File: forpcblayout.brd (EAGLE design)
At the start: 105.5 x 66.3 mm, 89 parts, among them J1 3x2 M, J2 S2B-PH-SM4-TB(LF)(SN), J3 629105136821, SW1 AYZ0202AGRLC, SW2 !RESET, T1 2N2222, T2 2N2222, T3 2N2222, T4 2N2222, U1 MCP73831, U2 MIC5219, U3 ATMEGA32U4-AUR, X2 16 MHz

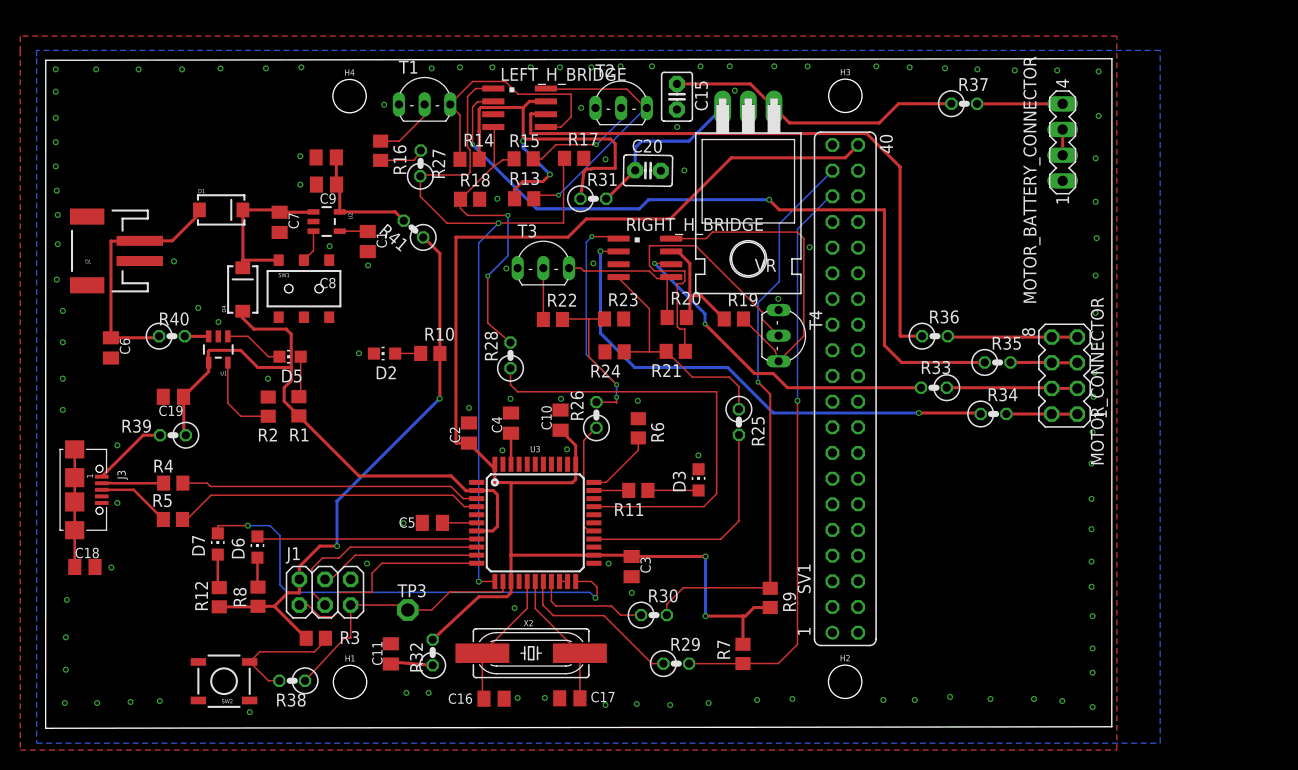
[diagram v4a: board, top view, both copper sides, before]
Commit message: Changed just about everything
Jk, changed wire widths, stitched properly, passed ERC as well as DRC
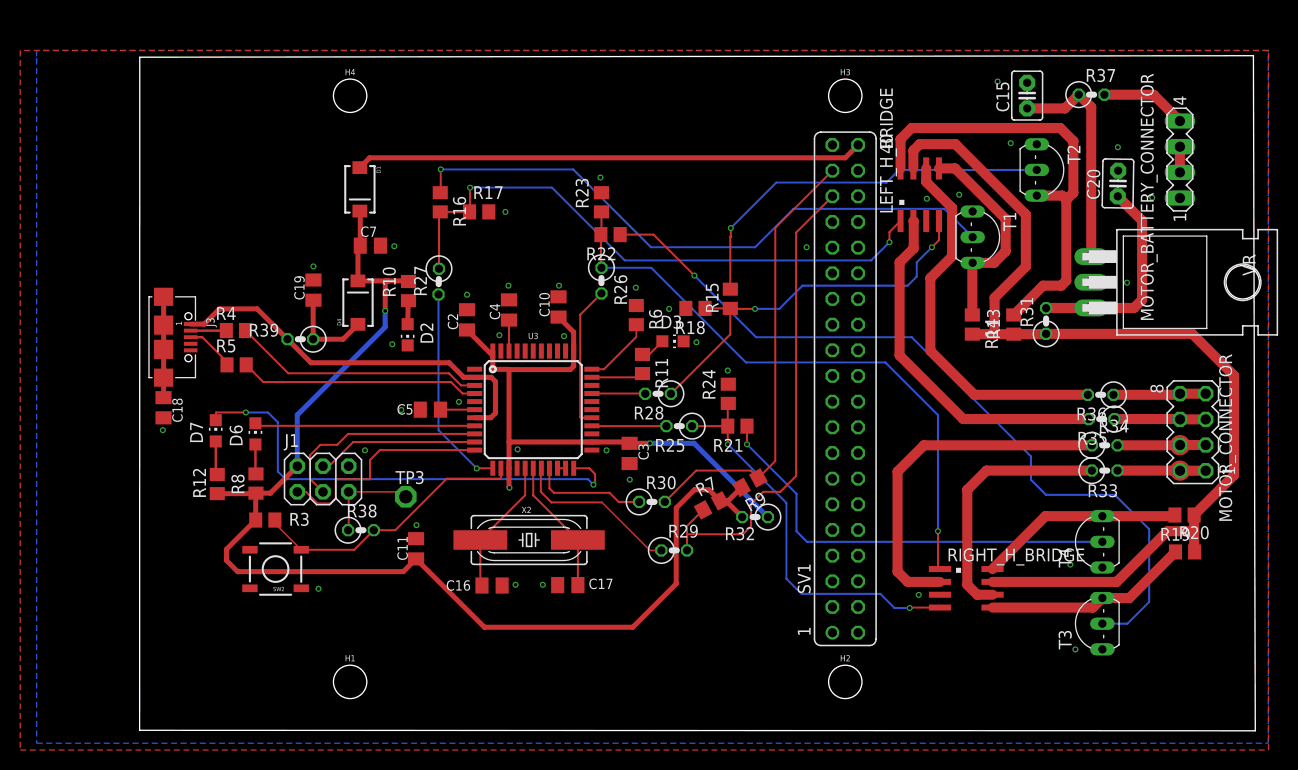
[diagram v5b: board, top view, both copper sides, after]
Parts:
- removed C1: 470p, rcl:C0805K
- removed C6, C8: 4.7u, rcl:C0805K
- removed C9: 100n, rcl:C0805K
- removed D5: GREEN, led:CHIP-LED0805
- removed J2: S2B-PH-SM4-TB(LF)(SN), SparkFun-Connectors:JST-2-SMD
- removed R1: 1K, rcl:R0805
- removed R2: 10K, rcl:R0805
- removed R40, R41: 0, rcl:0207/2V
- removed SW1: AYZ0202AGRLC, SparkFun-Electromechanical:AYZ0202
- removed U1: MCP73831, SparkFun-PowerIC:SOT23-5
- removed U2: MIC5219, SparkFun-PowerIC:SOT23-5
- MOTOR_BATTERY_CONNECTOR: value (none) -> MOTOR_BATTERY_CONNECTOR
- MOTOR_CONNECTOR: value (none) -> MOTOR_CONNECTOR
- R7, R9: value 1K -> 4.7K
- SV1: value (none) -> EXTENDED PIN HEADER
- moved T3 65.2 mm to (103.3, 10.3), turned to 90 degrees
- moved T1 57.3 mm to (93.0, 48.6), turned to 270 degrees
- moved R20 55.4 mm to (112.8, 17.4)
- moved R14 52.4 mm to (91.7, 40.0), turned to 270 degrees
- moved R13 50.0 mm to (95.8, 40.0), turned to 90 degrees
- moved R19 48.6 mm to (112.7, 21.1), turned to 180 degrees
- moved C20 46.5 mm to (106.1, 53.9), turned to 89.1 degrees
- moved R31 46.4 mm to (99.0, 40.3), turned to 90 degrees
- moved RIGHT_H_BRIDGE 45.6 mm to (91.1, 13.8)
- moved VR 44.7 mm to (113.6, 44.1), turned to 270 degrees
- moved T2 43.0 mm to (99.3, 55.2), turned to 270 degrees
- moved LEFT_H_BRIDGE 40.5 mm to (86.5, 52.8), turned to 0 degrees
- moved T4 35.9 mm to (103.3, 18.4), turned to 90 degrees
- moved C15 34.7 mm to (97.1, 62.6), turned to 90 degrees
- moved R32 34.6 mm to (70.2, 20.9), turned to 180 degrees
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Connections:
- net 7.4_FROM_BATT renamed 7.4_FROM_BATT_0
- removed net 3.3V: C8.1, C9.1, J1.2, R10.2, R12.2, R3.2, R41.1, R41.2, R8.2, U2.5
- removed net ACUATOR_POWER: LEFT_H_BRIDGE.7, R13.1, R14.2, R31.1
- removed net MCPPROG: R2.2, U1.5
- removed net MIC-BP: C1.1, U2.4
- removed net MIC-EN: SW1.2, U2.3
- removed net N$3: D5.A, R1.1
- removed net N$4: D5.C, U1.1
- removed net PWRIN: C7.1, D1.C, D4.C, SW1.1, U2.1
- removed net VBAT: R40.2, U1.3
- removed net V_BATT: C6.1, D1.A, J2.2, R40.1
- new net !RESET_0: J1.5, R38.1, TP3.TP
- new net 5V: C11.1, C7.1, D1.C, D4.C, J1.2, R10.2, R12.2, R3.2, R32.2, R7.2, R8.2, R9.2
- new net 5V_0: C10.1, C2.1, C3.1, R32.1, U3.14, U3.24, U3.34, U3.44
- new net ACTUATOR_POWER_0: LEFT_H_BRIDGE.7, R13.1, R14.2, R19.1, R20.2, R31.1, RIGHT_H_BRIDGE.7
- new net LEFT_MOTOR1_0: MOTOR_CONNECTOR.7, MOTOR_CONNECTOR.8, R36.1
- new net LEFT_MOTOR2_0: MOTOR_CONNECTOR.5, MOTOR_CONNECTOR.6, R35.1
- new net PWM_1_0: LEFT_H_BRIDGE.4, R15.2, R18.1, R28.1
- new net PWM_2_0: LEFT_H_BRIDGE.1, R16.2, R17.1, R27.1
- new net PWM_3_0: R21.2, R24.1, R25.1, RIGHT_H_BRIDGE.4
- new net PWM_4_0: R22.2, R23.1, R26.1, RIGHT_H_BRIDGE.1
- new net RIGHT_MOTOR1_0: MOTOR_CONNECTOR.1, MOTOR_CONNECTOR.2, R33.2
- new net RIGHT_MOTOR2_0: MOTOR_CONNECTOR.3, MOTOR_CONNECTOR.4, R34.2
- new net SCLK_0: R29.1, U3.18
- new net SDA_0: R30.1, U3.19
- new net VBUS_0: C19.1, D4.A, R39.1
- net !RESET: no longer J1.5, R38.1, TP3.TP
- net ACTUATOR_POWER: no longer R19.1, R20.2, RIGHT_H_BRIDGE.7
- net GND: no longer C1.2, C6.2, C8.2, C9.2, J2.1, R2.1, SW1.3, U1.2, U2.2
- net LEFT_MOTOR1: no longer MOTOR_CONNECTOR.7, MOTOR_CONNECTOR.8, R36.1
- net LEFT_MOTOR2: no longer MOTOR_CONNECTOR.5, MOTOR_CONNECTOR.6, R35.1
- net POWER_IN: now also D1.A; no longer C10.1, C11.1, C2.1, C3.1, R32.1, R32.2, R7.2, R9.2, U3.14, U3.24, U3.34, U3.44
- net PWM_1: no longer LEFT_H_BRIDGE.4, R15.2, R18.1, R28.1
- net PWM_2: no longer LEFT_H_BRIDGE.1, R16.2, R17.1, R27.1
- net PWM_3: no longer R21.2, R24.1, R25.1, RIGHT_H_BRIDGE.4
- net PWM_4: no longer R22.2, R23.1, R26.1, RIGHT_H_BRIDGE.1
- net RIGHT_MOTOR1: no longer MOTOR_CONNECTOR.3, MOTOR_CONNECTOR.4, R33.2
- net RIGHT_MOTOR2: no longer MOTOR_CONNECTOR.1, MOTOR_CONNECTOR.2, R34.2
- net SCLK: no longer R29.1, U3.18
- net SDA: no longer R30.1, U3.19
- net VBUS: no longer C19.1, D4.A, R1.2, R39.1, U1.4
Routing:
- net 5V: track 0.00 -> 119.2 mm, vias 0 -> 1
- net ACTUATOR_POWER_0: track 0.00 -> 97.9 mm
- net POWER_IN: track 144.7 -> 50.2 mm, vias 2 -> 0
- net N$22: track 5.08 -> 78.5 mm, vias 0 -> 1
- net 3.3V: track 71.6 -> 0.00 mm, vias 2 -> 0
- net PWM_1: track 76.5 -> 5.29 mm, vias 2 -> 0
- net PWM_2: track 82.5 -> 20.4 mm, vias 2 -> 1
- net PWM_4_0: track 0.00 -> 60.2 mm, vias 0 -> 1
- net 5V_0: track 0.00 -> 60.0 mm, vias 0 -> 2
- net PWM_2_0: track 0.00 -> 58.8 mm, vias 0 -> 2
- net N$12: track 6.52 -> 60.9 mm, vias 0 -> 1
- net LEFT_MOTOR2: track 80.9 -> 35.2 mm, vias 2 -> 0
- net ACUATOR_POWER: track 42.4 -> 0.00 mm, vias 2 -> 0
- net PWM_3: track 47.2 -> 7.39 mm
- net PWM_3_0: track 0.00 -> 39.7 mm, vias 0 -> 2
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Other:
- board size 105.5 x 66.3 mm -> 110.4 x 66.8 mm

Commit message: Made board slimmer, changed mask tab's limit, and included diff. DRU (Laen)
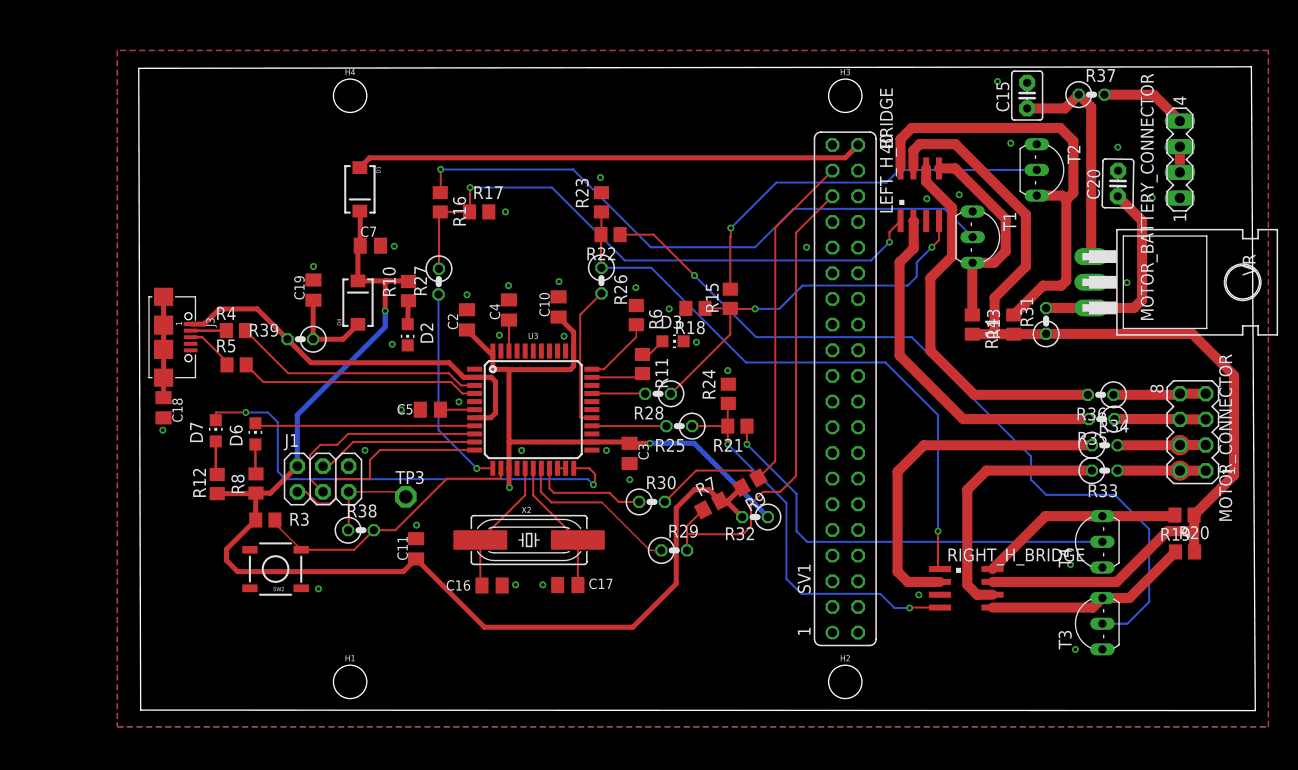
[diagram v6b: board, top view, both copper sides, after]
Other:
- board size 110.4 x 66.8 mm -> 110.5 x 63.7 mm
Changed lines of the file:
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@@
 <layer number="1" name="Top" color="4" fill="1" visible="yes" active="yes"/>
 <layer number="2" name="Route2" color="1" fill="3" visible="yes" active="yes"/>
-<layer number="3" name="Route3" color="4" fill="3" visible="no" active="yes"/>
-<layer number="4" name="Route4" color="1" fill="4" visible="no" active="yes"/>
-<layer number="5" name="Route5" color="4" fill="4" visible="no" active="yes"/>
-<layer number="6" name="Route6" color="1" fill="8" visible="no" active="yes"/>
-<layer number="7" name="Route7" color="4" fill="8" visible="no" active="yes"/>
-<layer number="8" name="Route8" color="1" fill="2" visible="no" active="yes"/>
-<layer number="9" name="Route9" color="4" fill="2" visible="no" active="yes"/>
-<layer number="10" name="Route10" color="1" fill="7" visible="no" active="yes"/>
-<layer number="11" name="Route11" color="4" fill="7" visible="no" active="yes"/>
-<layer number="12" name="Route12" color="1" fill="5" visible="no" active="yes"/>
-<layer number="13" name="Route13" color="4" fill="5" visible="no" active="yes"/>
-<layer number="14" name="Route14" color="1" fill="6" visible="no" active="yes"/>
-<layer number="15" name="Route15" color="4" fill="6" visible="no" active="yes"/>
+<layer number="3" name="Route3" color="4" fill="3" visible="yes" active="yes"/>
+<layer number="4" name="Route4" color="1" fill="4" visible="yes" active="yes"/>
+<layer number="5" name="Route5" color="4" fill="4" visible="yes" active="yes"/>
+<layer number="6" name="Route6" color="1" fill="8" visible="yes" active="yes"/>
+<layer number="7" name="Route7" color="4" fill="8" visible="yes" active="yes"/>
+<layer number="8" name="Route8" color="1" fill="2" visible="yes" active="yes"/>
+<layer number="9" name="Route9" color="4" fill="2" visible="yes" active="yes"/>
+<layer number="10" name="Route10" color="1" fill="7" visible="yes" active="yes"/>
+<layer number="11" name="Route11" color="4" fill="7" visible="yes" active="yes"/>
+<layer number="12" name="Route12" color="1" fill="5" visible="yes" active="yes"/>
+<layer number="13" name="Route13" color="4" fill="5" visible="yes" active="yes"/>
+<layer number="14" name="Route14" color="1" fill="6" visible="yes" active="yes"/>
+<layer number="15" name="Route15" color="4" fill="6" visible="yes" active="yes"/>
 <layer number="16" name="Bottom" color="1" fill="1" visible="yes" active="yes"/>
 <layer number="17" name="Pads" color="2" fill="1" visible="yes" active="yes"/>
@@
 <board>
 <plain>
-<wire x1="9.3" y1="-0.2" x2="119.7" y2="-0.25" width="0" layer="20"/>
-<wire x1="119.7" y1="-0.25" x2="119.513971875" y2="66.55493125" width="0" layer="20"/>
-<wire x1="119.513971875" y1="66.55493125" x2="9.313971875" y2="66.40493125" width="0" layer="20"/>
-<wire x1="9.313971875" y1="66.40493125" x2="9.3" y2="-0.2" width="0" layer="20"/>
+<wire x1="9.4" y1="1.8" x2="119.7" y2="1.75" width="0" layer="20"/>
+<wire x1="119.7" y1="1.75" x2="119.313971875" y2="65.45493125" width="0" layer="20"/>
+<wire x1="119.313971875" y1="65.45493125" x2="9.213971875" y2="65.30493125" width="0" layer="20"/>
+<wire x1="9.213971875" y1="65.30493125" x2="9.4" y2="1.8" width="0" layer="20"/>
 <dimension x1="0" y1="0" x2="56" y2="0" x3="28" y3="-8.8" textsize="1.778" layer="51" dtype="horizontal"/>
 <dimension x1="79.13843125" y1="62.5861125" x2="103.25" y2="4.6" x3="115" y3="33.59305625" textsize="1.778" layer="51" dtype="vertical"/>
@@
 </class>
 </classes>
-<designrules name="oshpark-2layer">
-<description language="en">&lt;b&gt;OSH Park Design Rules&lt;/b&gt;
+<designrules name="LaenPCBOrder *">
+<description language="de">&lt;b&gt;EAGLE Design Rules&lt;/b&gt;
 &lt;p&gt;
-Please make sure your boards conform to these design rules.
-&lt;/p&gt;
+Die Standard-Design-Rules sind so gewählt, dass sie für
+die meisten Anwendungen passen. Sollte ihre Platine
+besondere Anforderungen haben, treffen Sie die erforderlichen
+Einstellungen hier und speichern die Design Rules unter
+einem neuen Namen ab.</description>
+<description language="en">&lt;b&gt;Laen's PCB Order Design Rules&lt;/b&gt;
 &lt;p&gt;
-Note, that not all DRC settings must be set by the manufacturer. Several can be adjusted for the design, including those listed on our docs page here.
-&lt;a href=&quot;http://docs.oshpark.com/design-tools/eagle/design-rules-files/&quot;&gt;Adjustable Settings&lt;/a&gt;
-&lt;/p&gt;</description>
+Please make sure your boards conform to these design rules.</description>
 <param name="layerSetup" value="(1*16)"/>
-<param name="mtCopper" value="0.035559375mm 0.0356mm 0.0356mm 0.0356mm 0.0356mm 0.0356mm 0.0356mm 0.0356mm 0.0356mm 0.0356mm 0.0356mm 0.0356mm 0.0356mm 0.0356mm 0.0356mm 0.035559375mm"/>
-<param name="mtIsolate" value="1.6mm 0.1499mm 0.2007mm 0.1499mm 0.2007mm 0.1499mm 0.2007mm 0.1499mm 0.2007mm 0.1499mm 0.2007mm 0.1499mm 0.2007mm 0.1499mm 0.2007mm"/>
+<param name="mtCopper" value="0.0356mm 0.0356mm 0.0356mm 0.0356mm 0.0356mm 0.0356mm 0.0356mm 0.0356mm 0.0356mm 0.0356mm 0.0356mm 0.0356mm 0.0356mm 0.0356mm 0.0356mm 0.0356mm"/>
+<param name="mtIsolate" value="1.5011mm 0.1499mm 0.2007mm 0.1499mm 0.2007mm 0.1499mm 0.2007mm 0.1499mm 0.2007mm 0.1499mm 0.2007mm 0.1499mm 0.2007mm 0.1499mm 0.2007mm"/>
 <param name="mdWireWire" value="6mil"/>
 <param name="mdWirePad" value="6mil"/>
@@
 <param name="mdSmdStop" value="0mil"/>
 <param name="msWidth" value="6mil"/>
-<param name="msDrill" value="10mil"/>
-<param name="msMicroVia" value="10mil"/>
+<param name="msDrill" value="13mil"/>
+<param name="msMicroVia" value="13mil"/>
 <param name="msBlindViaRatio" value="0.5"/>
 <param name="rvPadTop" value="0.25"/>
@@
 <param name="rvMicroViaOuter" value="0.25"/>
 <param name="rvMicroViaInner" value="0.25"/>
-<param name="rlMinPadTop" value="5mil"/>
+<param name="rlMinPadTop" value="7mil"/>
 <param name="rlMaxPadTop" value="20mil"/>
-<param name="rlMinPadInner" value="5mil"/>
+<param name="rlMinPadInner" value="7mil"/>
 <param name="rlMaxPadInner" value="20mil"/>
-<param name="rlMinPadBottom" value="5mil"/>
+<param name="rlMinPadBottom" value="7mil"/>
 <param name="rlMaxPadBottom" value="20mil"/>
-<param name="rlMinViaOuter" value="5mil"/>
+<param name="rlMinViaOuter" value="7mil"/>
 <param name="rlMaxViaOuter" value="20mil"/>
-<param name="rlMinViaInner" value="5mil"/>
+<param name="rlMinViaInner" value="7mil"/>
 <param name="rlMaxViaInner" value="20mil"/>
-<param name="rlMinMicroViaOuter" value="5mil"/>
+<param name="rlMinMicroViaOuter" value="4mil"/>
 <param name="rlMaxMicroViaOuter" value="20mil"/>
-<param name="rlMinMicroViaInner" value="5mil"/>
+<param name="rlMinMicroViaInner" value="4mil"/>
 <param name="rlMaxMicroViaInner" value="20mil"/>
 <param name="psTop" value="-1"/>
@@
 <param name="mlMinCreamFrame" value="0mil"/>
 <param name="mlMaxCreamFrame" value="0mil"/>
-<param name="mlViaStopLimit" value="0mil"/>
+<param name="mlViaStopLimit" value="0.010159375mm"/>
 <param name="srRoundness" value="0"/>
 <param name="srMinRoundness" value="0mil"/>
@@
 <contactref element="C10" pad="2"/>
 <contactref element="C3" pad="2"/>
-<polygon width="0.1524" layer="1">
-<vertex x="-2.51333125" y="67.066159375"/>
-<vertex x="-2.51333125" y="-2.150109375"/>
-<vertex x="121.010321875" y="-2.150109375"/>
+<polygon width="0.2" layer="1">
+<vertex x="7.08666875" y="67.066159375"/>
+<vertex x="7.08666875" y="0.149890625"/>
+<vertex x="121.010321875" y="0.149890625"/>
 <vertex x="121.010321875" y="67.066159375"/>
 </polygon>
-<polygon width="0.1524" layer="16">
-<vertex x="-0.892809375" y="66.271140625"/>
-<vertex x="-0.892809375" y="-1.47446875"/>
-<vertex x="120.989340625" y="-1.47446875"/>
+<polygon width="0.2" layer="16">
+<vertex x="7.0983" y="67.077590625"/>
+<vertex x="7.0983" y="0.12553125"/>
+<vertex x="120.989340625" y="0.12553125"/>
 <vertex x="120.989340625" y="67.077590625"/>
-<vertex x="-0.9017" y="67.077590625"/>
-<vertex x="-0.9017" y="66.201290625"/>
 </polygon>
 <contactref element="C15" pad="2"/>
@@
 <via x="41.7" y="42.9" extent="1-16" drill="0.35"/>
 <via x="45.8" y="43.8" extent="1-16" drill="0.35"/>
-<via x="50.8" y="43.8" extent="1-16" drill="0.35"/>
+<via x="50.8" y="44.2" extent="1-16" drill="0.35"/>
 <via x="34.3" y="38" extent="1-16" drill="0.35"/>
 <via x="44.9" y="38.9" extent="1-16" drill="0.35"/>
@@
 <via x="40.9" y="32.3" extent="1-16" drill="0.35"/>
 <via x="35.2" y="31.5" extent="1-16" drill="0.35"/>
-<via x="46.7" y="27.6" extent="1-16" drill="0.35"/>
+<via x="47.1" y="27.5" extent="1-16" drill="0.35"/>
 <via x="31.6" y="27.5" extent="1-16" drill="0.35"/>
 <via x="11.6" y="29.5" extent="1-16" drill="0.35"/>

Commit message: Traces orthogonal to pads, schematic title, frame value, motor pin de-fucking.
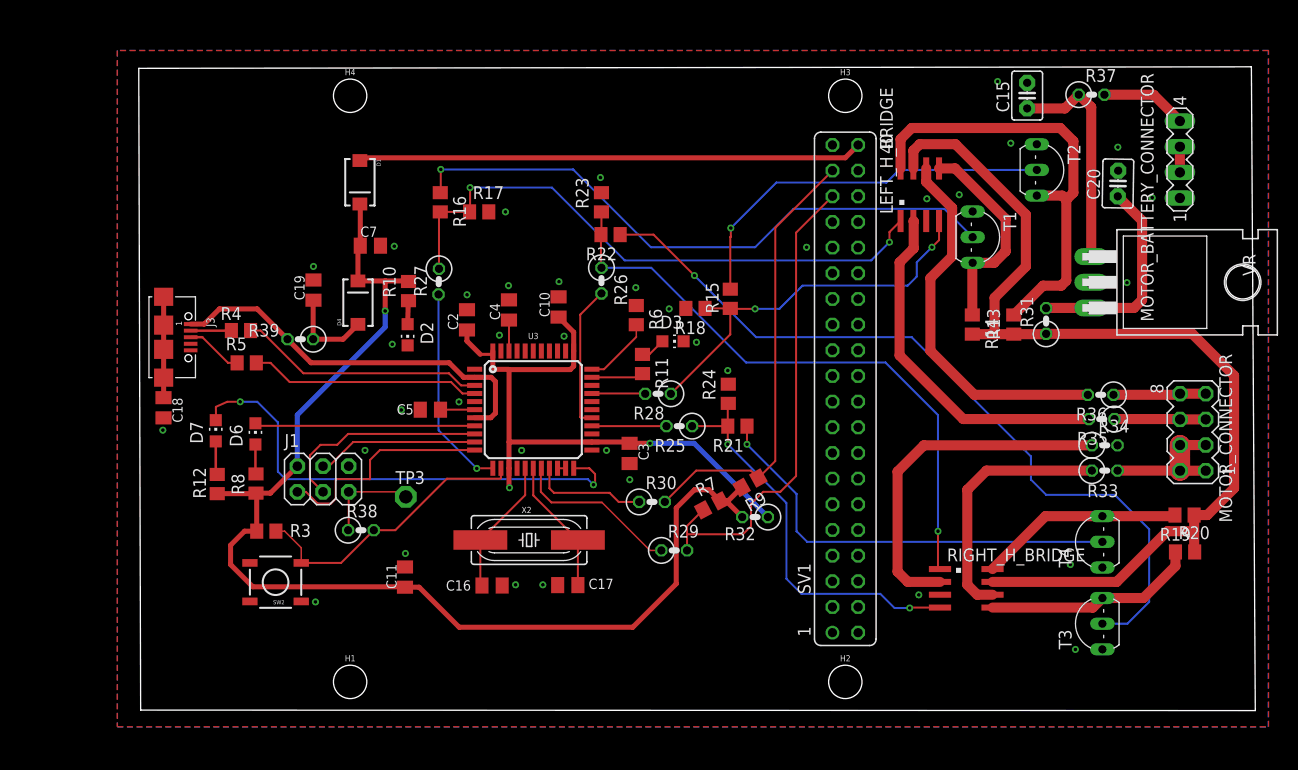
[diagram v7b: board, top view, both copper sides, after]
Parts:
- moved C11 3.01 mm to (35.6, 15.0)
- moved SW2 1.30 mm to (22.8, 14.5)
- moved R3 1.10 mm to (21.8, 19.5)
- moved R5 1.02 mm to (19.9, 36.2)
- moved D1 0.70 mm to (31.1, 54.0)
- moved R4 0.50 mm to (19.3, 39.4)
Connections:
- net RIGHT_MOTOR1_0: now also MOTOR_CONNECTOR.3, MOTOR_CONNECTOR.4; no longer MOTOR_CONNECTOR.1, MOTOR_CONNECTOR.2
- net RIGHT_MOTOR2_0: now also MOTOR_CONNECTOR.1, MOTOR_CONNECTOR.2; no longer MOTOR_CONNECTOR.3, MOTOR_CONNECTOR.4
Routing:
- net RIGHT_MOTOR2_0: track 8.74 -> 5.05 mm
- net RIGHT_MOTOR1_0: track 8.73 -> 11.2 mm
- net !RESET: track 27.7 -> 28.9 mm
- net TX_LED: track 47.5 -> 48.6 mm
- net D+: track 23.8 -> 22.9 mm
- net N$17: track 20.4 -> 21.2 mm
- net ACTUATOR_POWER_0: track 97.9 -> 98.7 mm
- net N$20: track 4.90 -> 5.65 mm
- net 5V_0: track 60.0 -> 60.6 mm
- net D-: track 24.9 -> 24.4 mm
